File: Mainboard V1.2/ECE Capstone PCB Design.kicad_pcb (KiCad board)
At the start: 2 copper layers, 114.9 x 66.9 mm, 72 parts, among them J1 1053131105, J2 1053131105, J3 Conn_01x40_Socket, U1 MCP2518FDT-H/SL, U2 MCP2542FD-E/SN, U5 TPS562201, U6 TPS61165DBV, U7 TPS562201

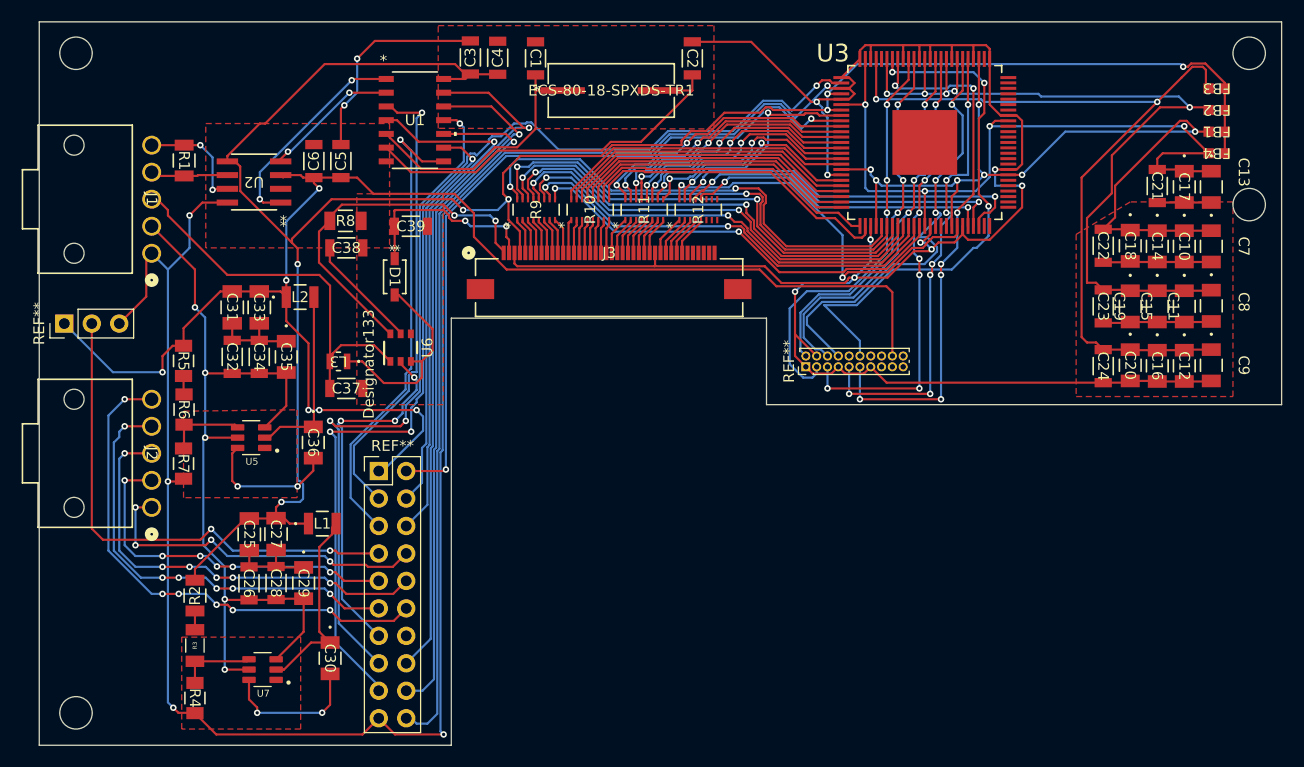
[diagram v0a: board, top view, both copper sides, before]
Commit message: Changed dev mode pin from 5V to 3.3V to comply with rasp pi high logic voltage. Changed some traces to remove any sharp angles and create more uniform lines where possible. Updated M2.5 screw cutouts to ensure they were accurate. Rounded the corners of the PCB to match that of the rasp pi. To do: Add 1mm of width to the bottom where the pi will be placed so that the pi lines up with the mainboard when placed. Move ferrite beads an appropriate distance away from the screw hole in the top right corner to maintain proper screw clearance.
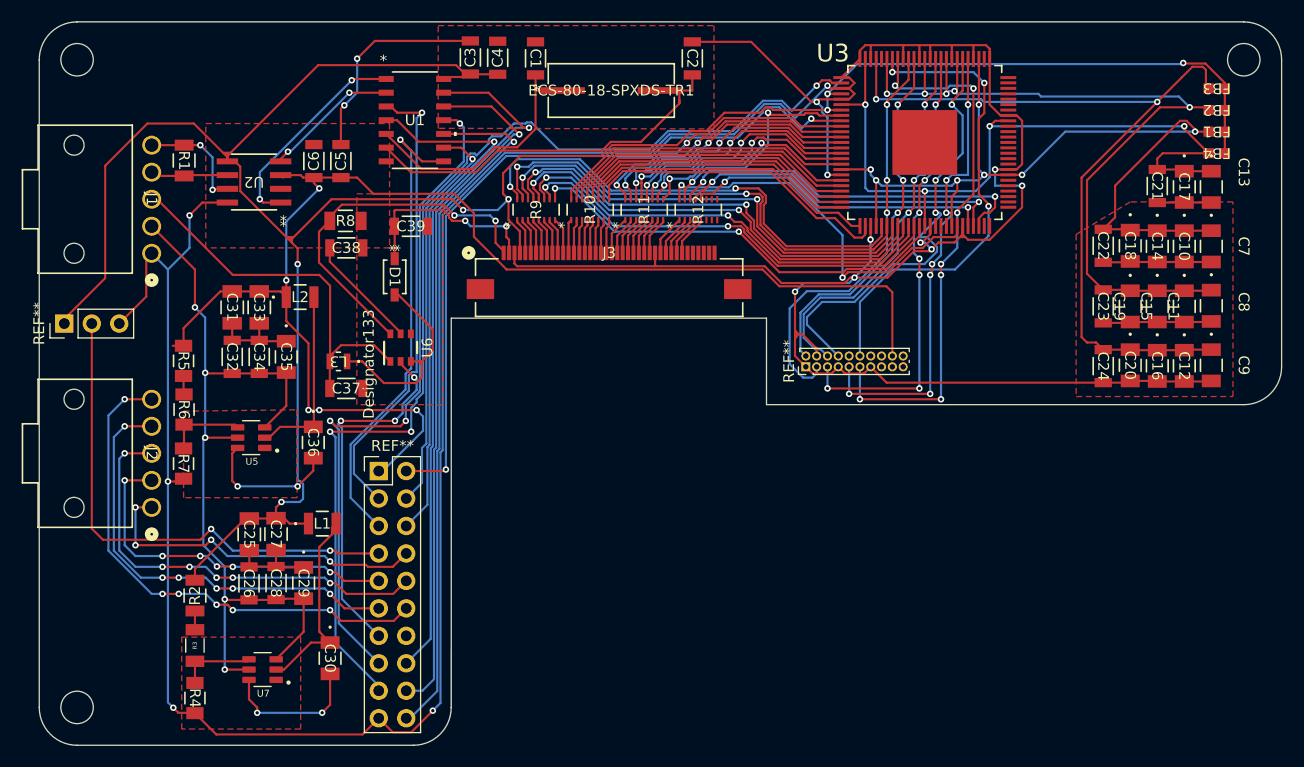
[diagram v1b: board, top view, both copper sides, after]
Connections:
- REF** pad 1: +5V -> +3.3V
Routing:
- net +3.3V: track 214.4 -> 244.7 mm
- net +5V: track 137.8 -> 124.0 mm, vias 6 -> 5
- net Net-(U3-RXC-): track 48.8 -> 44.3 mm
- net Net-(U1-OSC1): track 36.8 -> 40.0 mm
- net /GND: track 419.8 -> 417.9 mm
- net /Rasberry PI (SPI clock input): track 66.5 -> 64.8 mm
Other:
- outline, holes or cut-outs redrawn

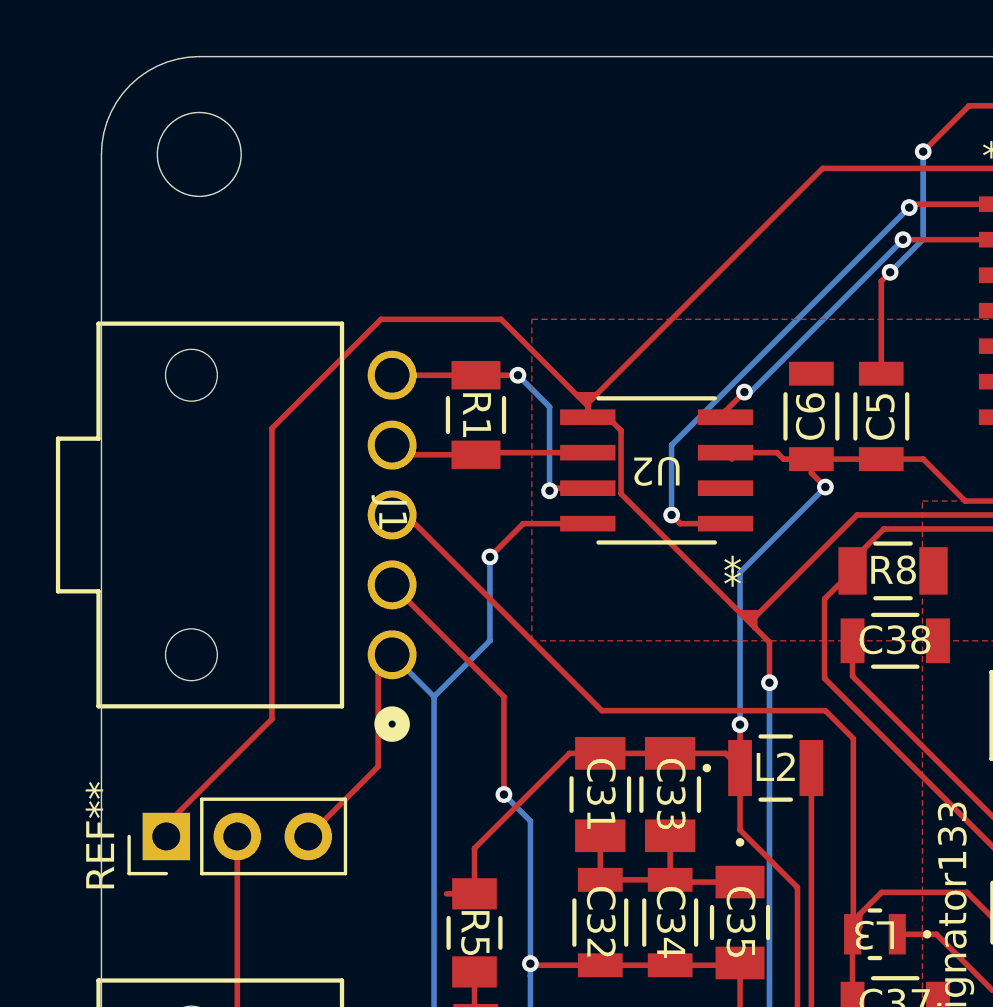
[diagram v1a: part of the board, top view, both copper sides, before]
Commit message: Fixed an issue with the dev mode pins connection to 3.3V rail
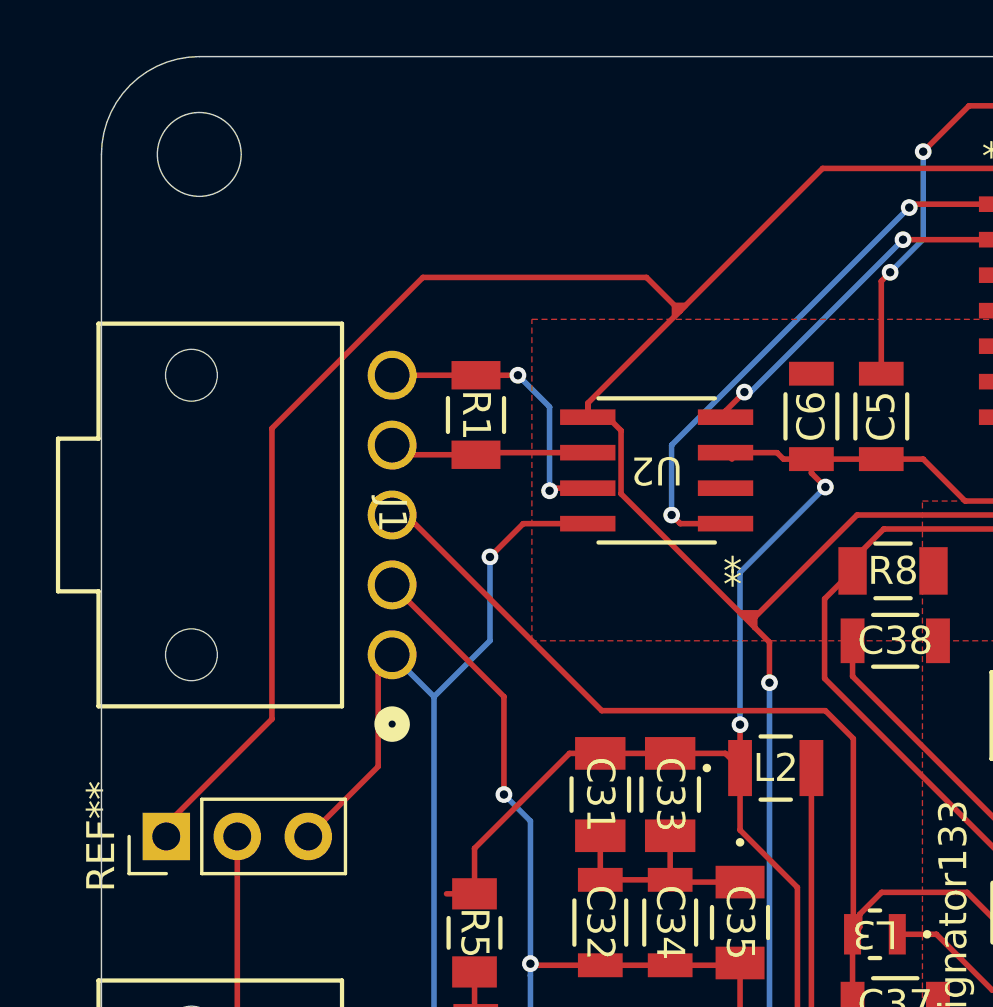
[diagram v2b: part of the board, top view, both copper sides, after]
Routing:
- net +3.3V: track 244.7 -> 247.8 mm
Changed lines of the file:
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@@
 	(gr_poly
 		(pts
-			(xy 139.6 59.2) (xy 140.3 59.2) (xy 140 59.5)
+			(xy 143.1 56.4) (xy 143.1 56) (xy 143.5 56)
 		)
 		(stroke
@@
 	)
 	(segment
+		(start 148.4 51.1)
+		(end 143.3 56.2)
+		(width 0.2)
+		(layer "F.Cu")
+		(net 1)
+	)
+	(segment
+		(start 128.7 60.4)
+		(end 134.1 55)
+		(width 0.2)
+		(layer "F.Cu")
+		(net 1)
+	)
+	(segment
+		(start 124.92 74.58)
+		(end 128.7 70.8)
+		(width 0.2)
+		(layer "F.Cu")
+		(net 1)
+	)
+	(segment
 		(start 144.5 93)
 		(end 144.5 92)
@@
 	)
 	(segment
+		(start 143.3 56.2)
+		(end 140 59.5)
+		(width 0.2)
+		(layer "F.Cu")
+		(net 1)
+	)
+	(segment
 		(start 146.5 69.5)
 		(end 146.5 68.0527)
@@
 	)
 	(segment
+		(start 124.92 75)
+		(end 124.92 74.58)
+		(width 0.2)
+		(layer "F.Cu")
+		(net 1)
+	)
+	(segment
 		(start 142.0268 97.4732)
 		(end 142 97.5)
@@
 	)
 	(segment
-		(start 128.7 60.4)
-		(end 128.7 70.8)
-		(width 0.2)
-		(layer "F.Cu")
-		(net 1)
-	)
-	(segment
 		(start 228.45 50.95)
 		(end 230.45 50.95)
@@
 	)
 	(segment
+		(start 142.1 55)
+		(end 143.3 56.2)
+		(width 0.2)
+		(layer "F.Cu")
+		(net 1)
+	)
+	(segment
 		(start 165.5 63)
 		(end 165.5 61.095472)
@@
 	)
 	(segment
-		(start 124.92 74.58)
-		(end 124.92 75)
-		(width 0.2)
-		(layer "F.Cu")
-		(net 1)
-	)
-	(segment
 		(start 142 97.5)
 		(end 142.027801 97.472199)
@@
 	)
 	(segment
-		(start 148.4 51.1)
-		(end 140 59.5)
-		(width 0.2)
-		(layer "F.Cu")
-		(net 1)
-	)
-	(segment
 		(start 162.472199 51.916597)
 		(end 161.972199 51.916597)
@@
 	)
 	(segment
-		(start 140 59.6)
-		(end 136.9 56.5)
+		(start 134.1 55)
+		(end 142.1 55)
 		(width 0.2)
 		(layer "F.Cu")
@@
 	)
 	(segment
-		(start 128.7 70.8)
-		(end 124.92 74.58)
-		(width 0.2)
-		(layer "F.Cu")
-		(net 1)
-	)
-	(segment
 		(start 145.3058 97.5508)
 		(end 147.0522 97.5508)
@@
 	)
 	(segment
-		(start 136.9 56.5)
-		(end 132.6 56.5)
-		(width 0.2)
-		(layer "F.Cu")
-		(net 1)
-	)
-	(segment
 		(start 144.5 93)
 		(end 145.255 93)
@@
 	)
 	(segment
+		(start 128.7 70.8)
+		(end 128.7 60.4)
+		(width 0.2)
+		(layer "F.Cu")
+		(net 1)
+	)
+	(segment
 		(start 140.4473 74.974701)
 		(end 140.4473 76.5527)
@@
 		(width 0.2)
 		(layer "F.Cu")
-		(net 1)
-	)
-	(segment
-		(start 132.6 56.5)
-		(end 128.7 60.4)
-		(width 0.2)
-		(layer "F.Cu")

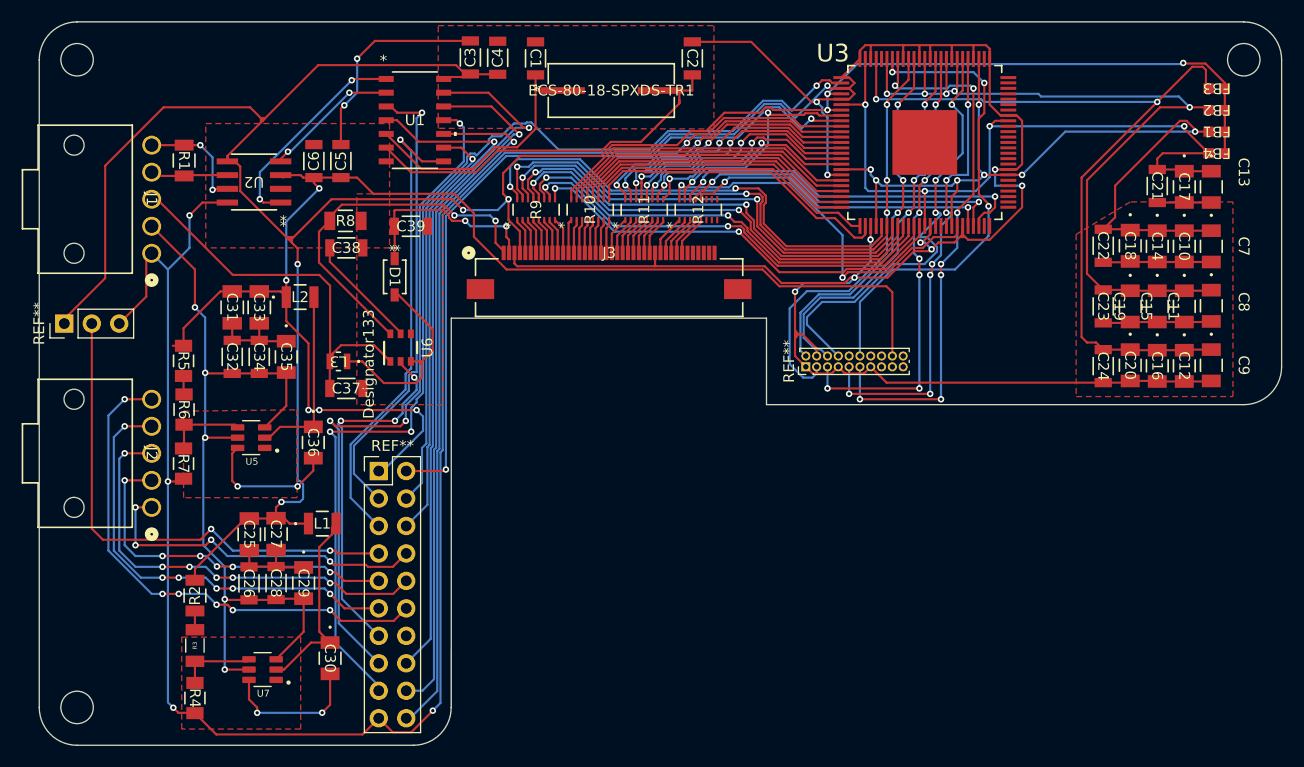
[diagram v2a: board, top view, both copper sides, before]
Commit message: Added 1mm to the bottom of the PCB where the rasp pi sits. Moved the ferrite beads to give more room around the screw mounts. Cleaned up the silk screen layer.
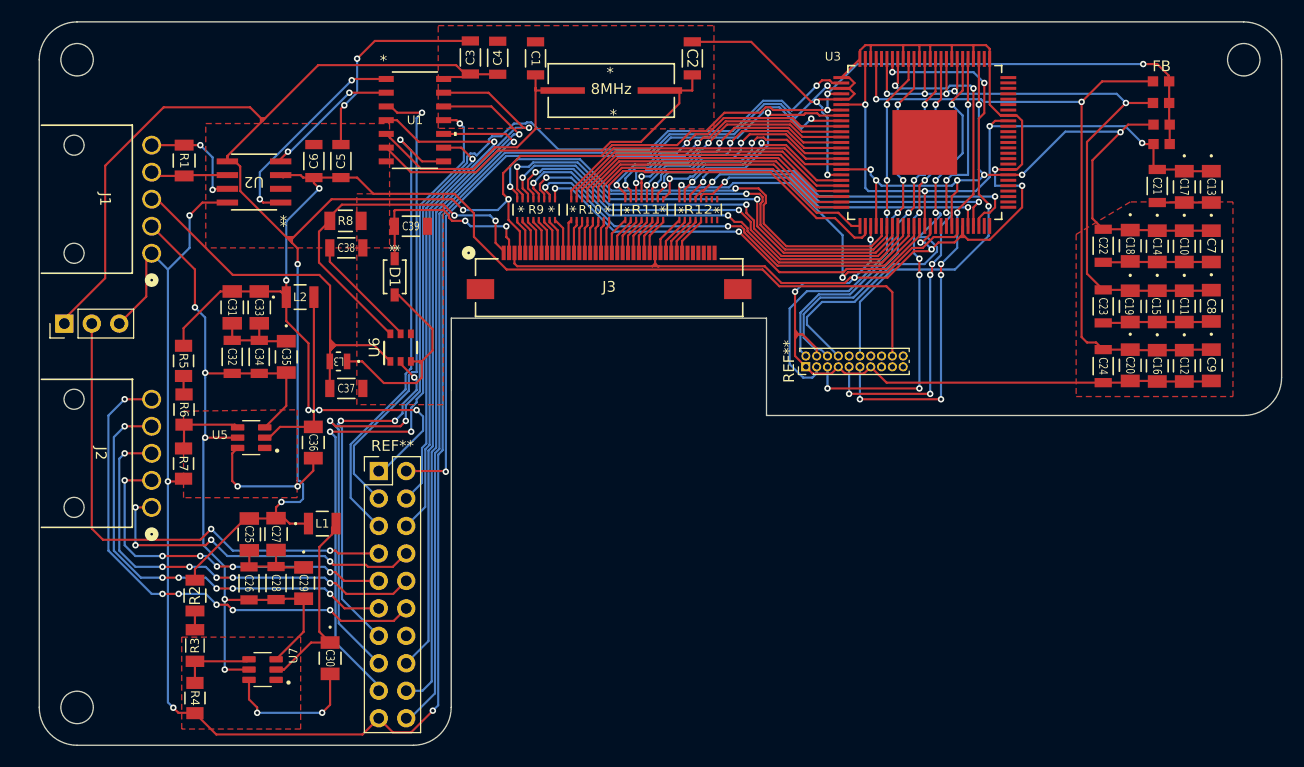
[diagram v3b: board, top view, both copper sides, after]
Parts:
- moved FB 5.19 mm to (226.4, 52.6)
- moved FB2 5.19 mm to (226.4, 54.6)
- moved FB4 5.17 mm to (226.4, 58.4)
- moved FB1 5.14 mm to (226.4, 56.6)
- renumbered ECS-80-18-SPXDS-TR1 to 8MHz, FB3 to FB
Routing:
- net Net-(U3-PVDD): track 74.6 -> 64.4 mm
- net Net-(U3-OVDD): track 81.3 -> 72.1 mm
- net Net-(U3-DVDD): track 68.4 -> 59.3 mm
- net Net-(U3-AVDD): track 76.2 -> 67.3 mm
- net +3.3V: track 247.8 -> 242.1 mm
- net +5V: track 124.0 -> 123.0 mm
- net /GND: track 417.9 -> 418.8 mm
- net 12V: track 36.4 -> 35.7 mm
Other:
- outline, holes or cut-outs redrawn
